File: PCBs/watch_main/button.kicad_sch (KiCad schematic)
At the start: 1 part, among them SW1501 EVP-AEJB2A

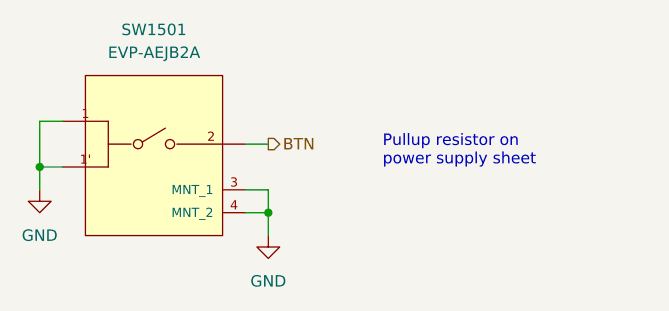
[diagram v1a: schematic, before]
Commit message: Schematic finished and BOM started
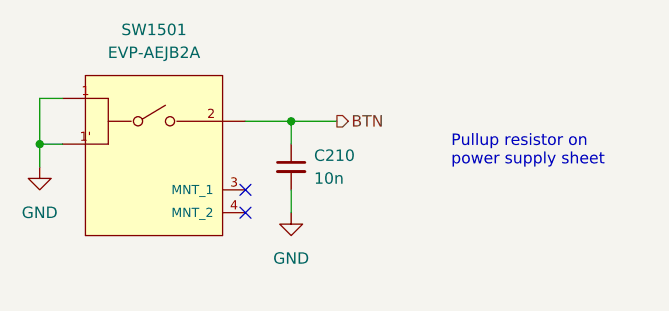
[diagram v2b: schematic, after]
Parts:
- added C210: 10n, Capacitor_SMD:C_0402_1005Metric, symbol Device:C_Small
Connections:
- net BTN: now also C210.1
- net GND: now also C210.2; no longer SW1501.3 (MNT_1), SW1501.4 (MNT_2)
- no-connect marks 0 -> 2
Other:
- title: (none) -> Watch Button
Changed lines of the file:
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@@
 (kicad_sch (version 20230121) (generator eeschema)
   (paper "A4")
-  (junction (at 149.86 104.14) (diameter 0) (color 0 0 0 0)
-  )
-  (junction (at 124.46 99.06) (diameter 0) (color 0 0 0 0)
-  )
-  (wire (pts (xy 124.46 93.98) (xy 127 93.98))
-    (stroke (width 0) (type default))
-  )
-  (wire (pts (xy 124.46 101.6) (xy 124.46 99.06))
-    (stroke (width 0) (type default))
-  )
-  (wire (pts (xy 149.86 101.6) (xy 149.86 104.14))
-    (stroke (width 0) (type default))
-  )
-  (wire (pts (xy 149.86 104.14) (xy 147.32 104.14))
-    (stroke (width 0) (type default))
-  )
-  (wire (pts (xy 124.46 99.06) (xy 127 99.06))
-    (stroke (width 0) (type default))
-  )
-  (wire (pts (xy 149.86 106.68) (xy 149.86 104.14))
-    (stroke (width 0) (type default))
-  )
-  (wire (pts (xy 124.46 99.06) (xy 124.46 93.98))
-    (stroke (width 0) (type default))
-  )
-  (wire (pts (xy 149.86 96.52) (xy 147.32 96.52))
-    (stroke (width 0) (type default))
-  )
-  (wire (pts (xy 147.32 101.6) (xy 149.86 101.6))
-    (stroke (width 0) (type default))
-  )
-  (text "Pullup resistor on\npower supply sheet" (at 162.56 99.06 0)
-    (effects (font (size 1.27 1.27)) (justify left bottom))
-  )
-  (hierarchical_label "BTN" (shape output) (at 149.86 96.52 0) (fields_autoplaced)
+  (title_block
+    (title "Watch Button")
+    (date "2023-12-20")
+    (rev "1")
+    (comment 1 "Checked by Ben Smith on 20/12/23")
+  )
+  (junction (at 152.4 93.98) (diameter 0) (color 0 0 0 0)
+  )
+  (junction (at 124.46 96.52) (diameter 0) (color 0 0 0 0)
+  )
+  (no_connect (at 147.32 104.14))
+  (no_connect (at 147.32 101.6))
+  (wire (pts (xy 152.4 93.98) (xy 152.4 96.52))
+    (stroke (width 0) (type default))
+  )
+  (wire (pts (xy 152.4 104.14) (xy 152.4 101.6))
+    (stroke (width 0) (type default))
+  )
+  (wire (pts (xy 124.46 91.44) (xy 127 91.44))
+    (stroke (width 0) (type default))
+  )
+  (wire (pts (xy 124.46 99.06) (xy 124.46 96.52))
+    (stroke (width 0) (type default))
+  )
+  (wire (pts (xy 152.4 93.98) (xy 147.32 93.98))
+    (stroke (width 0) (type default))
+  )
+  (wire (pts (xy 124.46 96.52) (xy 127 96.52))
+    (stroke (width 0) (type default))
+  )
+  (wire (pts (xy 124.46 96.52) (xy 124.46 91.44))
+    (stroke (width 0) (type default))
+  )
+  (wire (pts (xy 157.48 93.98) (xy 152.4 93.98))
+    (stroke (width 0) (type default))
+  )
+  (text "Pullup resistor on\npower supply sheet" (at 170.18 99.06 0)
+    (effects (font (size 1.27 1.27)) (justify left bottom) (href "#2"))
+  )
+  (hierarchical_label "BTN" (shape output) (at 157.48 93.98 0) (fields_autoplaced)
     (effects (font (size 1.27 1.27)) (justify left))
   )
@@
     )
   )
-  (symbol (lib_id "power:GND") (at 149.86 106.68 0) (unit 1)
+  (symbol (lib_id "power:GND") (at 152.4 104.14 0) (unit 1)
     (in_bom yes) (on_board yes) (dnp no) (fields_autoplaced)
-    (property "Reference" "#PWR01502" (at 149.86 113.03 0)
-      (effects (font (size 1.27 1.27)) hide)
-    )
-    (property "Value" "GND" (at 149.86 111.76 0)
-      (effects (font (size 1.27 1.27)))
-    )
-    (property "Footprint" "" (at 149.86 106.68 0)
-      (effects (font (size 1.27 1.27)) hide)
-    )
-    (property "Datasheet" "" (at 149.86 106.68 0)
+    (property "Reference" "#PWR01502" (at 152.4 110.49 0)
+      (effects (font (size 1.27 1.27)) hide)
+    )
+    (property "Value" "GND" (at 152.4 109.22 0)
+      (effects (font (size 1.27 1.27)))
+    )
+    (property "Footprint" "" (at 152.4 104.14 0)
+      (effects (font (size 1.27 1.27)) hide)
+    )
+    (property "Datasheet" "" (at 152.4 104.14 0)
       (effects (font (size 1.27 1.27)) hide)
     )
@@
     )
   )
-  (symbol (lib_id "power:GND") (at 124.46 101.6 0) (unit 1)
+  (symbol (lib_id "power:GND") (at 124.46 99.06 0) (unit 1)
     (in_bom yes) (on_board yes) (dnp no) (fields_autoplaced)
-    (property "Reference" "#PWR01501" (at 124.46 107.95 0)
-      (effects (font (size 1.27 1.27)) hide)
-    )
-    (property "Value" "GND" (at 124.46 106.68 0)
-      (effects (font (size 1.27 1.27)))
-    )
-    (property "Footprint" "" (at 124.46 101.6 0)
-      (effects (font (size 1.27 1.27)) hide)
-    )
-    (property "Datasheet" "" (at 124.46 101.6 0)
+    (property "Reference" "#PWR01501" (at 124.46 105.41 0)
+      (effects (font (size 1.27 1.27)) hide)
+    )
+    (property "Value" "GND" (at 124.46 104.14 0)
+      (effects (font (size 1.27 1.27)))
+    )
+    (property "Footprint" "" (at 124.46 99.06 0)
+      (effects (font (size 1.27 1.27)) hide)
+    )
+    (property "Datasheet" "" (at 124.46 99.06 0)
       (effects (font (size 1.27 1.27)) hide)
     )
@@
         )
       )
+    )
+  )
+  (symbol (lib_id "Device:C_Small") (at 152.4 99.06 0) (unit 1)
+    (in_bom yes) (on_board yes) (dnp no)
+    (property "Reference" "C210" (at 154.94 97.7963 0)
+      (effects (font (size 1.27 1.27)) (justify left))
+    )
+    (property "Value" "10n" (at 154.94 100.3363 0)
+      (effects (font (size 1.27 1.27)) (justify left))
+    )
+    (property "Footprint" "Capacitor_SMD:C_0402_1005Metric" (at 152.4 99.06 0)
+      (effects (font (size 1.27 1.27)) hide)
+    )
+    (property "Datasheet" "~" (at 152.4 99.06 0)
+      (effects (font (size 1.27 1.27)) hide)
+    )
+    (pin "1")
+    (pin "2")
+    (instances
+      (project "watch_main"
+        (path "/b008648a-c7cf-4e14-8a0a-b9314d757b4a/8f996a8c-7777-4a55-b361-37cede76953f"
+          (reference "C210") (unit 1)
+        )
+        (path "/b008648a-c7cf-4e14-8a0a-b9314d757b4a/007c56e9-a012-43a8-8c47-a9871f01caa0"
+          (reference "C1501") (unit 1)
+        )
+      )
